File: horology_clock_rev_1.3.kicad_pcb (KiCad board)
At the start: 2 copper layers, 100 x 100 mm, 42 parts, among them J1 Conn_01x36, J10 Conn_01x08, J11 Screw_Terminal_01x02, J12 Conn_01x02, J13 Conn_01x04, J14 Conn_01x10, J2 Conn_01x36, J3 Screw_Terminal_01x02, J4 Screw_Terminal_01x02, J5 Screw_Terminal_01x02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

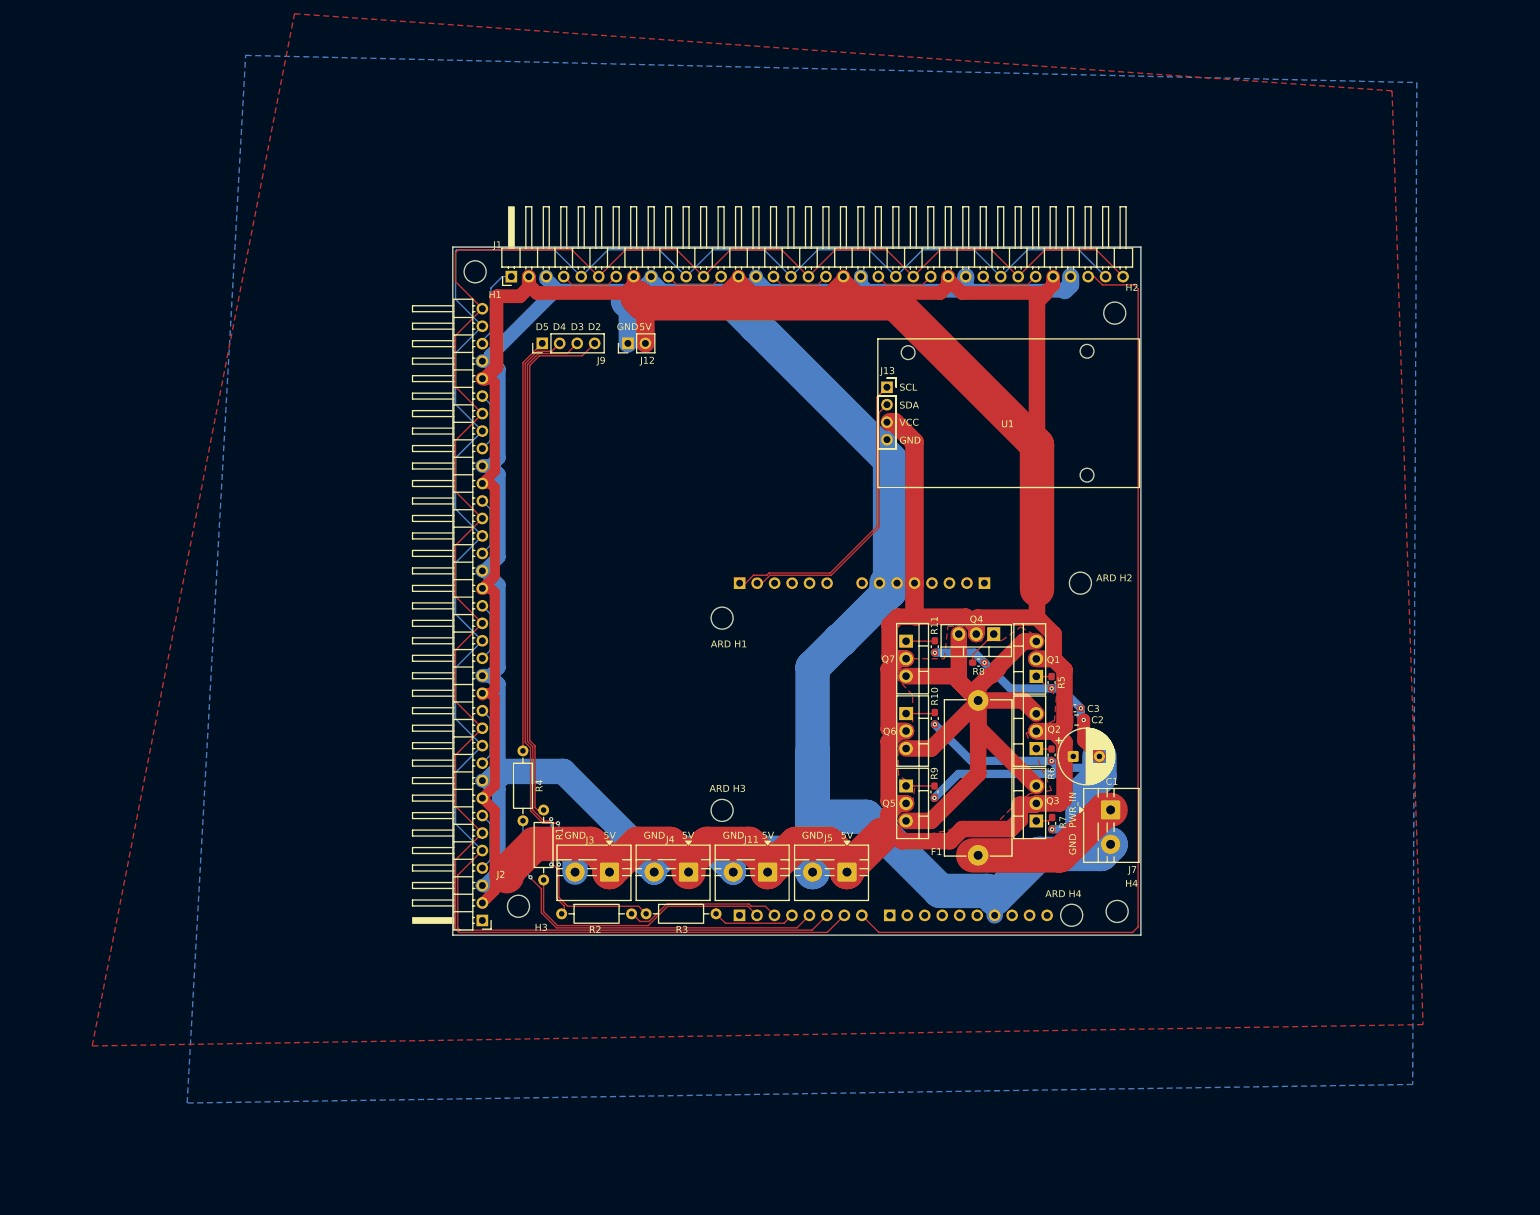
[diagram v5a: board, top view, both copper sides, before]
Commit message: Moved Arduino such that mounting holes for all components dont intersect other each others footprints.
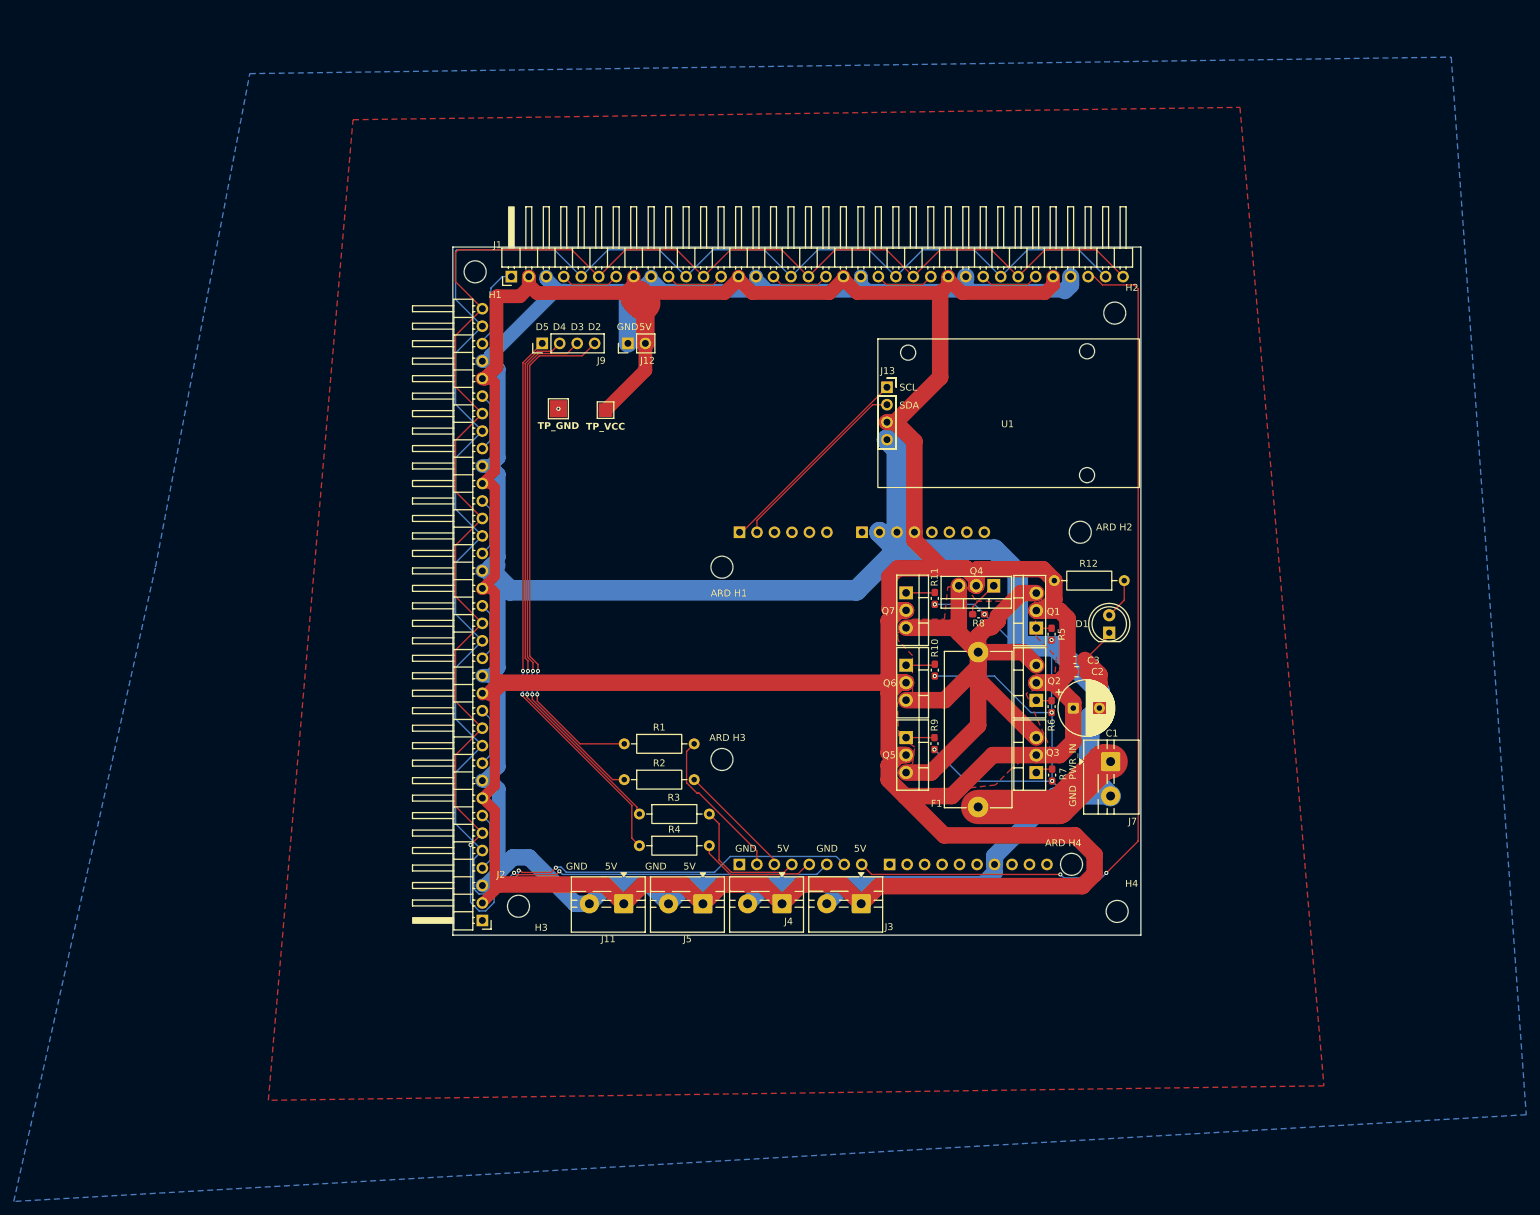
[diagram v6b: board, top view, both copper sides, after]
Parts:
- added D1: LED, LED_THT:LED_D5.0mm, F.Cu at (176.3, 105.2)
- added R12: 1kΩ, Resistor_THT:R_Axial_DIN0207_L6.3mm_D2.5mm_P10.16mm_Horizontal, F.Cu at (178.5, 97.7)
- added TP1: TestPoint, TestPoint:TestPoint_Pad_2.5x2.5mm, F.Cu at (96.3, 72.7)
- added TP2: TestPoint, TestPoint:TestPoint_Pad_2.0x2.0mm, F.Cu at (103.2, 72.9)
- moved J3 36.9 mm to (140.3, 144.6)
- moved R4 21.8 mm to (108.1, 136.2), turned to 0 degrees
- moved R2 21.5 mm to (105.9, 126.6)
- moved J5 21.4 mm to (117.3, 144.7)
- moved J11 21.4 mm to (105.8, 144.6)
- moved J8 19.3 mm to (140.4, 90.6), turned to -90 degrees
- moved R1 15.2 mm to (105.9, 121.4), turned to 0 degrees
- moved R3 14.5 mm to (108.1, 131.6)
- moved J4 14.3 mm to (128.8, 144.6)
- moved J10 7.40 mm to (122.6, 138.9)
- moved A1 7.40 mm to (158.2, 90.7)
- moved J6 7.40 mm to (122.6, 90.7)
- moved J14 7.40 mm to (144.4, 138.9)
- moved C3 7.03 mm to (171.4, 109.2)
- moved F1 7.03 mm to (157.3, 130.6)
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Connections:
- J8 pad 2: unconnected-(J8-Pin_2-Pad2) -> GND
- J8 pad 3: unconnected-(J8-Pin_3-Pad3) -> GND
- J8 pad 4: unconnected-(J8-Pin_4-Pad4) -> +5V
- J8 pad 5: +5V -> unconnected-(J8-Pin_5-Pad5)
- J8 pad 6: GND -> unconnected-(J8-Pin_6-Pad6)
- J8 pad 7: GND -> unconnected-(J8-Pin_7-Pad7)
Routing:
- net Net-(J10-Pin_5): track 55.1 -> 17.6 mm, vias 1 -> 0
- net 7SEG_DATA: track 100.8 -> 78.6 mm
- net DOTS_DATA: track 60.4 -> 81.1 mm, vias 0 -> 2
- net GND: track 599.0 -> 619.0 mm, vias 9 -> 8
- net BINARY_DATA: track 91.9 -> 75.7 mm
- net Net-(J10-Pin_2): track 38.2 -> 22.4 mm
- net RTC_SCL: track 44.2 -> 30.2 mm
- net RTC_SDA: track 39.4 -> 27.6 mm
- net +5V: track 611.1 -> 600.2 mm
- net MAX_DIN: track 142.2 -> 131.4 mm, vias 0 -> 2
- net MAX_CS: track 284.6 -> 277.2 mm, vias 0 -> 2
- net Net-(J10-Pin_4): track 12.1 -> 19.1 mm
- net Net-(D1-A): track 0.00 -> 5.94 mm
- net Net-(J10-Pin_3): track 23.0 -> 17.1 mm
- net MAX_CLK: track 290.4 -> 288.1 mm, vias 0 -> 3
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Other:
- board text added: "TP_GND"
- board text added: "TP_VCC"
- board text removed: "J3"
- board text removed: "MAX_CLK_D7"
- board text removed: "MAX_CS_D6"
- board text removed: "MAX_DIN_D8"
- board text removed: "VCC"

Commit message: Minor changes.
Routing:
- net MAX_DIN: vias 2 -> 1
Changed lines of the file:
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@@
 			(layer "F.Fab")
 		)
+		(fp_text user "4"
+			(at -17.32 2.32 0)
+			(unlocked yes)
+			(layer "F.Fab")
+			(effects
+				(font
+					(size 0.5 0.5)
+					(thickness 0.05)
+				)
+			)
+		)
 		(fp_text user "${REFERENCE}"
 			(at 0.2 3.4 0)
@@
 			)
 		)
+		(fp_text user "3"
+			(at -17.32 -0.22 0)
+			(unlocked yes)
+			(layer "F.Fab")
+			(effects
+				(font
+					(size 0.5 0.5)
+					(thickness 0.05)
+				)
+			)
+		)
 		(fp_text user "2"
 			(at -17.32 -2.76 0)
@@
 			(layer "Dwgs.User")
 			(pts
-				(xy 142.725 64.95) (xy 146.125 64.55)
+				(xy 173.125 65.35) (xy 173.125 81.35)
 			)
-			(height -4.4)
-			(orientation 0)
+			(height 0)
+			(orientation 1)
 			(format
 				(prefix "")
@@
 				(keep_text_aligned yes)
 			)
-			(gr_text "3.4"
-				(at 144.425 59.45 0)
+			(gr_text "16"
+				(at 172.025 73.35 90)
 				(layer "Dwgs.User")
 				(effects
@@
 			(layer "Dwgs.User")
 			(pts
-				(xy 173.125 65.35) (xy 173.125 81.35)
+				(xy 180.825 63.55) (xy 174.125 63.45)
 			)
-			(height 0)
-			(orientation 1)
+			(height -2.9)
+			(orientation 0)
 			(format
 				(prefix "")
@@
 				(keep_text_aligned yes)
 			)
-			(gr_text "16"
-				(at 172.025 73.35 90)
+			(gr_text "6.7"
+				(at 177.475 59.55 0)
 				(layer "Dwgs.User")
 				(effects
@@
 			(layer "Dwgs.User")
 			(pts
-				(xy 180.825 63.55) (xy 174.125 63.45)
+				(xy 142.725 64.95) (xy 146.125 64.55)
 			)
-			(height -2.9)
+			(height -4.4)
 			(orientation 0)
 			(format
@@
 				(keep_text_aligned yes)
 			)
-			(gr_text "6.7"
-				(at 177.475 59.55 0)
+			(gr_text "3.4"
+				(at 144.425 59.45 0)
 				(layer "Dwgs.User")
 				(effects
@@
 			(drill 2.2)
 			(layers "*.Cu" "*.Mask")
+			(clearance 0.2)
 		)
 		(pad "" np_thru_hole circle
@@
 			(drill 2.2)
 			(layers "*.Cu" "*.Mask")
+			(clearance 0.2)
 		)
 		(pad "" np_thru_hole circle
@@
 			(drill 2.2)
 			(layers "*.Cu" "*.Mask")
+			(clearance 0.2)
 		)
 		(embedded_fonts no)
@@
 	)
 	(footprint "MountingHole:MountingHole_3.2mm_M3"
-		(locked yes)
 		(layer "F.Cu")
-		(at 84.2 52.8)
+		(at 84.25 52.8)
 		(descr "Mounting Hole 3.2mm, M3, no annular, generated by kicad-footprint-generator mountinghole.py")
 		(tags "mountinghole M3")
@@
 	)
 	(footprint "MountingHole:MountingHole_3.2mm_M3"
-		(locked yes)
 		(layer "F.Cu")
 		(at 177.5 145.75)
@@
 	)
 	(segment
-		(start 175.37 54.71)
-		(end 174.16 53.5)
-		(width 0.2)
-		(layer "F.Cu")
-		(net 9)
-	)
-	(segment
-		(start 180.549 135.537802)
-		(end 180.549 135.5)
+		(start 140.38 138.92)
+		(end 141.84 140.38)
 		(width 0.2)
 		(layer "F.Cu")
 		(net 9)
 	)
-	(segment
-		(start 179.96 54.71)
-		(end 175.37 54.71)
-		(width 0.2)
-		(layer "F.Cu")
+	(via
+		(at 169.25 140.38)
+		(size 0.6)
+		(drill 0.3)
+		(layers "F.Cu" "B.Cu")
 		(net 9)
 	)
 	(segment
-		(start 174.16 53.5)
+		(start 174.431 54.651)
 		(end 173.28 53.5)
 		(width 0.2)
-		(layer "F.Cu")
+		(layer "B.Cu")
 		(net 9)
 	)
 	(segment
-		(start 180.549 135.5)
+		(start 180.549 135.537802)
 		(end 180.549 55.299)
 		(width 0.2)
-		(layer "F.Cu")
+		(layer "B.Cu")
 		(net 9)
 	)
 	(segment
-		(start 140.38 138.92)
-		(end 141.84 140.38)
+		(start 179.901 54.651)
+		(end 174.431 54.651)
 		(width 0.2)
-		(layer "F.Cu")
+		(layer "B.Cu")
 		(net 9)
 	)
 	(segment
-		(start 175.925 140.161802)
-		(end 180.549 135.537802)
+		(start 169.735 140.865)
+		(end 175.221802 140.865)
 		(width 0.2)
-		(layer "F.Cu")
+		(layer "B.Cu")
 		(net 9)
 	)
 	(segment
-		(start 180.549 55.299)
-		(end 179.96 54.71)
+		(start 175.221802 140.865)
+		(end 180.549 135.537802)
 		(width 0.2)
-		(layer "F.Cu")
-		(net 9)
-	)
-	(via
-		(at 175.925 140.161802)
-		(size 0.6)
-		(drill 0.3)
-		(layers "F.Cu" "B.Cu")
-		(net 9)
-	)
-	(via
-		(at 169.25 140.38)
-		(size 0.6)
-		(drill 0.3)
-		(layers "F.Cu" "B.Cu")
+		(layer "B.Cu")
 		(net 9)
 	)
@@
 	)
 	(segment
-		(start 169.735 140.865)
-		(end 175.221802 140.865)
-		(width 0.2)
-		(layer "B.Cu")
-		(net 9)
-	)
-	(segment
-		(start 175.221802 140.865)
-		(end 175.925 140.161802)
+		(start 180.549 55.299)
+		(end 179.901 54.651)
 		(width 0.2)
 		(layer "B.Cu")
@@
 	)
 	(segment
-		(start 89.46 53.5)
-		(end 88.15 53.5)
+		(start 88.5 53.5)
+		(end 86.5 55.5)
 		(width 0.2)
 		(layer "B.Cu")
@@
 	)
 	(segment
-		(start 85.25 62.8)
-		(end 85.25 63.245)
+		(start 86.5 61.55)
+		(end 85.25 62.8)
 		(width 0.2)
 		(layer "B.Cu")
@@
 	)
 	(segment
-		(start 88.15 53.5)
-		(end 86.5 55.15)
+		(start 89.46 53.5)
+		(end 88.5 53.5)
 		(width 0.2)
 		(layer "B.Cu")
@@
 	)
 	(segment
-		(start 86.5 55.15)
-		(end 86.5 61.55)
+		(start 85.25 62.8)
+		(end 85.25 63.245)
 		(width 0.2)
 		(layer "B.Cu")
@@
 	)
 	(segment
-		(start 86.5 61.55)
-		(end 85.25 62.8)
+		(start 86.5 55.5)
+		(end 86.5 61.55)
 		(width 0.2)
 		(layer "B.Cu")

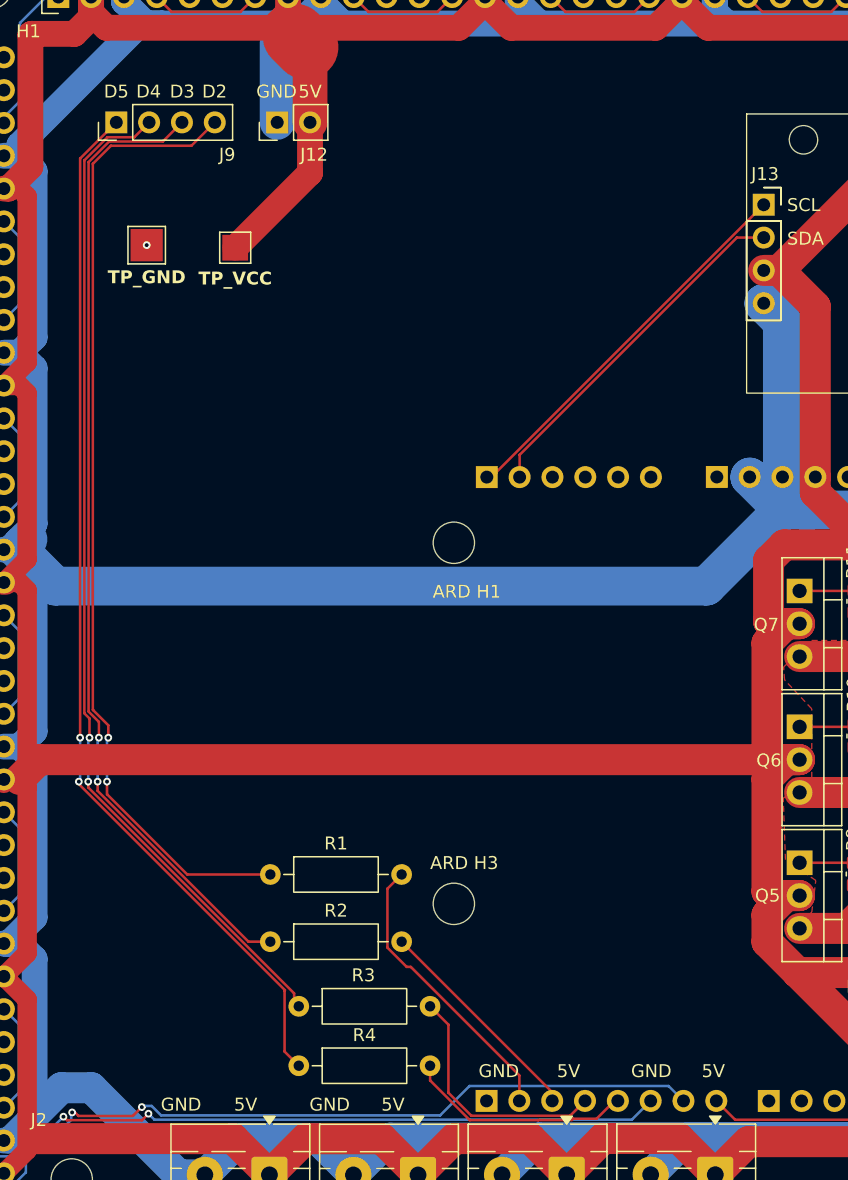
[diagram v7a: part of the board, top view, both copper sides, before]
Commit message: Moved Pin 1 to Pin 8 to avoid Serial Issues.
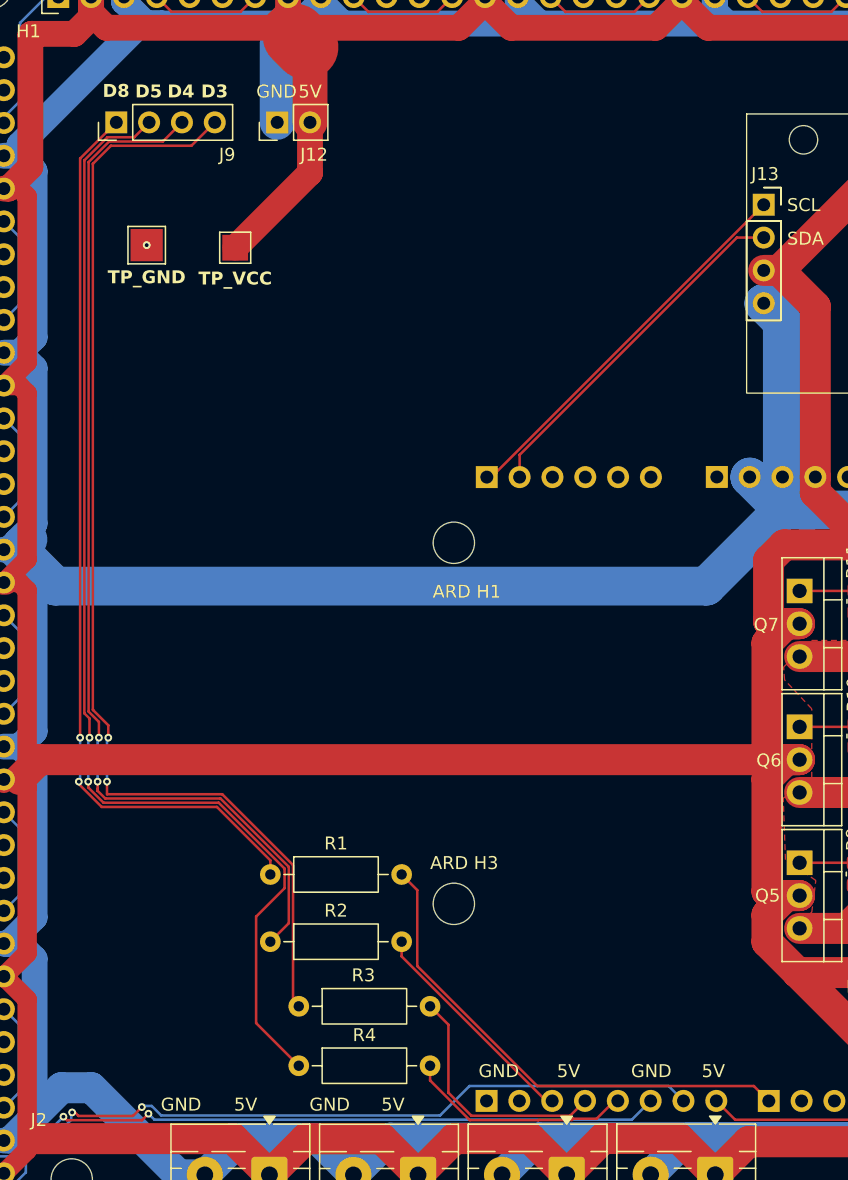
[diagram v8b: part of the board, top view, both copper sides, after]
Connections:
- J10 pad 2: Net-(J10-Pin_2) -> unconnected-(J10-Pin_2-Pad2)
- J14 pad 1: unconnected-(J14-3.3V-Pad1) -> Net-(J14-3.3V)
- J9 pad 1: DOTS_DATA -> HEART_BEAT_DATA
- J9 pad 2: 7SEG_DATA -> DOTS_DATA
- J9 pad 4: HEART_BEAT_DATA -> 7SEG_DATA
- R1 pad 2: Net-(J10-Pin_2) -> Net-(J14-3.3V)
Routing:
- net Net-(J14-3.3V): track 0.00 -> 39.1 mm
- net Net-(J10-Pin_2): track 22.4 -> 0.00 mm
- net 7SEG_DATA: track 78.6 -> 87.9 mm
- net DOTS_DATA: track 81.1 -> 90.3 mm
- net BINARY_DATA: track 75.7 -> 81.3 mm
- net HEART_BEAT_DATA: track 75.3 -> 70.6 mm
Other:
- board text added: "D8"
- board text removed: "D2"
